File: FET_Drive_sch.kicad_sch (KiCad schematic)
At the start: 14 parts, among them Q15 S8550, Q16 S8050_SMD, Q17 S8050_SMD, Q18 S8050_SMD

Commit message: moree wiring done, shrank board slightly. Unsure whether 4 layer is necessary
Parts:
- added C24, C25: 10u, Capacitor_SMD:C_0603_1608Metric, symbol Device:C_Small
- renumbered D7 to D6, Q18 to Q10, Q15 to Q6, Q16 to Q8, Q17 to Q9, R28 to R19, R54 to R22, R55 to R23, R56 to R24, R57 to R25, R58 to R27, R62 to R59, R63 to R60, R64 to R61
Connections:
- net GND: now also C24.2, C25.2
- new net +12V: C24.1, C25.1
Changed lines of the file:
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@@
   (symbol (lib_id "Device:R_Small_US") (at 168.275 84.455 0) (mirror y)
     (in_bom yes) (on_board yes)
-    (property "Reference" "R56" (id 0) (at 171.45 85.725 0))
+    (property "Reference" "R24" (id 0) (at 171.45 85.725 0))
     (property "Value" "3.3M" (id 1) (at 164.465 84.455 0))
     (property "Footprint" "Resistor_SMD:R_0402_1005Metric" (id 2) (at 168.275 84.455 0)
@@
   (symbol (lib_id "Device:R_Small_US") (at 113.665 86.995 90)
     (in_bom yes) (on_board yes)
-    (property "Reference" "R57" (id 0) (at 113.665 82.1395 90))
+    (property "Reference" "R25" (id 0) (at 113.665 82.1395 90))
     (property "Value" "4k7" (id 1) (at 113.665 84.9146 90))
     (property "Footprint" "Resistor_SMD:R_0402_1005Metric" (id 2) (at 113.665 86.995 0)
@@
     (pin "2")
   )
+  (symbol (lib_id "Device:C_Small") (at 113.03 62.865 0)
+    (in_bom yes) (on_board yes) (fields_autoplaced)
+    (property "Reference" "C25" (id 0) (at 115.3541 61.9628 0)
+      (effects (font (size 1.27 1.27)) (justify left))
+    )
+    (property "Value" "10u" (id 1) (at 115.3541 64.7379 0)
+      (effects (font (size 1.27 1.27)) (justify left))
+    )
+    (property "Footprint" "Capacitor_SMD:C_0603_1608Metric" (id 2) (at 113.03 62.865 0)
+      (effects (font (size 1.27 1.27)) hide)
+    )
+    (property "Datasheet" "~" (id 3) (at 113.03 62.865 0)
+      (effects (font (size 1.27 1.27)) hide)
+    )
+    (property "Populate" "Yes" (id 4) (at 113.03 62.865 0)
+      (effects (font (size 1.27 1.27)) hide)
+    )
+    (property "Extended" "0" (id 5) (at 113.03 62.865 0)
+      (effects (font (size 1.27 1.27)) hide)
+    )
+    (property "LCSC" "C96446" (id 6) (at 113.03 62.865 0)
+      (effects (font (size 1.27 1.27)) hide)
+    )
+    (property "Price" "0.03" (id 7) (at 113.03 62.865 0)
+      (effects (font (size 1.27 1.27)) hide)
+    )
+    (pin "1")
+    (pin "2")
+  )
   (symbol (lib_id "MyDevices:S8050_SMD") (at 137.795 92.075 0)
     (in_bom yes) (on_board yes) (fields_autoplaced)
-    (property "Reference" "Q18" (id 0) (at 141.3764 91.1665 0)
+    (property "Reference" "Q10" (id 0) (at 141.3764 91.1665 0)
       (effects (font (size 1.27 1.27)) (justify left))
     )
@@
   (symbol (lib_id "Device:R_Small_US") (at 155.575 68.58 90)
     (in_bom yes) (on_board yes)
-    (property "Reference" "R62" (id 0) (at 155.575 63.7245 90))
+    (property "Reference" "R59" (id 0) (at 155.575 63.7245 90))
     (property "Value" "100R" (id 1) (at 165.1 66.4996 90))
     (property "Footprint" "Resistor_SMD:R_0402_1005Metric" (id 2) (at 155.575 68.58 0)
@@
     (pin "2")
   )
+  (symbol (lib_id "power:+12V") (at 102.235 60.325 0)
+    (in_bom yes) (on_board yes) (fields_autoplaced)
+    (property "Reference" "#PWR0112" (id 0) (at 102.235 64.135 0)
+      (effects (font (size 1.27 1.27)) hide)
+    )
+    (property "Value" "+12V" (id 1) (at 102.235 56.7205 0))
+    (property "Footprint" "" (id 2) (at 102.235 60.325 0)
+      (effects (font (size 1.27 1.27)) hide)
+    )
+    (property "Datasheet" "" (id 3) (at 102.235 60.325 0)
+      (effects (font (size 1.27 1.27)) hide)
+    )
+    (pin "1")
+  )
   (symbol (lib_id "MyDevices:S8050_SMD") (at 146.685 86.995 0)
     (in_bom yes) (on_board yes) (fields_autoplaced)
-    (property "Reference" "Q17" (id 0) (at 150.2664 86.0865 0)
+    (property "Reference" "Q9" (id 0) (at 150.2664 86.0865 0)
       (effects (font (size 1.27 1.27)) (justify left))
     )
@@
   (symbol (lib_id "Device:R_Small_US") (at 155.575 81.915 90)
     (in_bom yes) (on_board yes)
-    (property "Reference" "R54" (id 0) (at 155.575 77.0595 90))
+    (property "Reference" "R22" (id 0) (at 155.575 77.0595 90))
     (property "Value" "100R" (id 1) (at 165.1 79.8346 90))
     (property "Footprint" "Resistor_SMD:R_0402_1005Metric" (id 2) (at 155.575 81.915 0)
@@
   (symbol (lib_id "MyDevices:S8550") (at 146.685 72.39 0)
     (in_bom yes) (on_board yes) (fields_autoplaced)
-    (property "Reference" "Q15" (id 0) (at 150.2664 71.4815 0)
+    (property "Reference" "Q6" (id 0) (at 150.2664 71.4815 0)
       (effects (font (size 1.27 1.27)) (justify left))
     )
@@
   (symbol (lib_id "Device:R_Small_US") (at 139.065 84.455 180)
     (in_bom yes) (on_board yes)
-    (property "Reference" "R55" (id 0) (at 136.525 85.725 0))
+    (property "Reference" "R23" (id 0) (at 136.525 85.725 0))
     (property "Value" "4k7" (id 1) (at 132.08 83.82 0))
     (property "Footprint" "Resistor_SMD:R_0402_1005Metric" (id 2) (at 139.065 84.455 0)
@@
     (pin "2")
   )
+  (symbol (lib_id "Device:C_Small") (at 102.235 62.865 0)
+    (in_bom yes) (on_board yes) (fields_autoplaced)
+    (property "Reference" "C24" (id 0) (at 104.5591 61.9628 0)
+      (effects (font (size 1.27 1.27)) (justify left))
+    )
+    (property "Value" "10u" (id 1) (at 104.5591 64.7379 0)
+      (effects (font (size 1.27 1.27)) (justify left))
+    )
+    (property "Footprint" "Capacitor_SMD:C_0603_1608Metric" (id 2) (at 102.235 62.865 0)
+      (effects (font (size 1.27 1.27)) hide)
+    )
+    (property "Datasheet" "~" (id 3) (at 102.235 62.865 0)
+      (effects (font (size 1.27 1.27)) hide)
+    )
+    (property "Populate" "Yes" (id 4) (at 102.235 62.865 0)
+      (effects (font (size 1.27 1.27)) hide)
+    )
+    (property "Extended" "0" (id 5) (at 102.235 62.865 0)
+      (effects (font (size 1.27 1.27)) hide)
+    )
+    (property "LCSC" "C96446" (id 6) (at 102.235 62.865 0)
+      (effects (font (size 1.27 1.27)) hide)
+    )
+    (property "Price" "0.03" (id 7) (at 102.235 62.865 0)
+      (effects (font (size 1.27 1.27)) hide)
+    )
+    (pin "1")
+    (pin "2")
+  )
+  (symbol (lib_id "power:+12V") (at 113.03 60.325 0)
+    (in_bom yes) (on_board yes) (fields_autoplaced)
+    (property "Reference" "#PWR0110" (id 0) (at 113.03 64.135 0)
+      (effects (font (size 1.27 1.27)) hide)
+    )
+    (property "Value" "+12V" (id 1) (at 113.03 56.7205 0))
+    (property "Footprint" "" (id 2) (at 113.03 60.325 0)
+      (effects (font (size 1.27 1.27)) hide)
+    )
+    (property "Datasheet" "" (id 3) (at 113.03 60.325 0)
+      (effects (font (size 1.27 1.27)) hide)
+    )
+    (pin "1")
+  )
   (symbol (lib_id "Device:D_Zener_Small") (at 175.26 84.455 270)
     (in_bom yes) (on_board yes)
-    (property "Reference" "D7" (id 0) (at 177.038 83.5465 90)
+    (property "Reference" "D6" (id 0) (at 177.038 83.5465 90)
       (effects (font (size 1.27 1.27)) (justify left))
     )
@@
     (pin "2")
   )
+  (symbol (lib_id "power:GND") (at 102.235 65.405 0)
+    (in_bom yes) (on_board yes) (fields_autoplaced)
+    (property "Reference" "#PWR0113" (id 0) (at 102.235 71.755 0)
+      (effects (font (size 1.27 1.27)) hide)
+    )
+    (property "Value" "GND" (id 1) (at 102.235 69.9675 0))
+    (property "Footprint" "" (id 2) (at 102.235 65.405 0)
+      (effects (font (size 1.27 1.27)) hide)
+    )
+    (property "Datasheet" "" (id 3) (at 102.235 65.405 0)
+      (effects (font (size 1.27 1.27)) hide)
+    )
+    (pin "1")
+  )
   (symbol (lib_id "MyDevices:S8050_SMD") (at 123.825 86.995 0)
     (in_bom yes) (on_board yes) (fields_autoplaced)
-    (property "Reference" "Q16" (id 0) (at 127.4064 86.0865 0)
+    (property "Reference" "Q8" (id 0) (at 127.4064 86.0865 0)
       (effects (font (size 1.27 1.27)) (justify left))
     )
@@
     (pin "3")
   )
+  (symbol (lib_id "power:GND") (at 113.03 65.405 0)
+    (in_bom yes) (on_board yes) (fields_autoplaced)
+    (property "Reference" "#PWR0111" (id 0) (at 113.03 71.755 0)
+      (effects (font (size 1.27 1.27)) hide)
+    )
+    (property "Value" "GND" (id 1) (at 113.03 69.9675 0))
+    (property "Footprint" "" (id 2) (at 113.03 65.405 0)
+      (effects (font (size 1.27 1.27)) hide)
+    )
+    (property "Datasheet" "" (id 3) (at 113.03 65.405 0)
+      (effects (font (size 1.27 1.27)) hide)
+    )
+    (pin "1")
+  )
   (symbol (lib_id "Device:R_Small_US") (at 155.575 77.47 90)
     (in_bom yes) (on_board yes)
-    (property "Reference" "R64" (id 0) (at 155.575 72.6145 90))
+    (property "Reference" "R61" (id 0) (at 155.575 72.6145 90))
     (property "Value" "100R" (id 1) (at 165.1 75.3896 90))
     (property "Footprint" "Resistor_SMD:R_0402_1005Metric" (id 2) (at 155.575 77.47 0)
@@
   (symbol (lib_id "Device:R_Small_US") (at 113.665 95.885 90)
     (in_bom yes) (on_board yes)
-    (property "Reference" "R58" (id 0) (at 113.665 91.0295 90))
+    (property "Reference" "R27" (id 0) (at 113.665 91.0295 90))
     (property "Value" "4k7" (id 1) (at 113.665 93.8046 90))
     (property "Footprint" "Resistor_SMD:R_0402_1005Metric" (id 2) (at 113.665 95.885 0)
@@
   (symbol (lib_id "Device:R_Small_US") (at 135.255 72.39 90)
     (in_bom yes) (on_board yes)
-    (property "Reference" "R28" (id 0) (at 135.255 67.5345 90))
+    (property "Reference" "R19" (id 0) (at 135.255 67.5345 90))
     (property "Value" "4k7" (id 1) (at 135.255 70.3096 90))
     (property "Footprint" "Resistor_SMD:R_0402_1005Metric" (id 2) (at 135.255 72.39 0)
@@
   (symbol (lib_id "Device:R_Small_US") (at 155.575 73.025 90)
     (in_bom yes) (on_board yes)
-    (property "Reference" "R63" (id 0) (at 155.575 68.1695 90))
+    (property "Reference" "R60" (id 0) (at 155.575 68.1695 90))
     (property "Value" "100R" (id 1) (at 165.1 70.9446 90))
     (property "Footprint" "Resistor_SMD:R_0402_1005Metric" (id 2) (at 155.575 73.025 0)

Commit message: got lazy, went 4 layer. Some of layer 3 done. progressing. Mainly committing for board chronological how to sake. Added Caps on the TM1620
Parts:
- renumbered C24 to C26, C25 to C27, D6 to D7, Q6 to Q15, Q8 to Q16, Q9 to Q17, Q10 to Q18, R19 to R28, R22 to R54, R23 to R55, R24 to R56, R25 to R57, R27 to R58, R59 to R62, R60 to R63, R61 to R64
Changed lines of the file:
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@@
   (symbol (lib_id "Device:R_Small_US") (at 168.275 84.455 0) (mirror y)
     (in_bom yes) (on_board yes)
-    (property "Reference" "R24" (id 0) (at 171.45 85.725 0))
+    (property "Reference" "R56" (id 0) (at 171.45 85.725 0))
     (property "Value" "3.3M" (id 1) (at 164.465 84.455 0))
     (property "Footprint" "Resistor_SMD:R_0402_1005Metric" (id 2) (at 168.275 84.455 0)
@@
   (symbol (lib_id "Device:R_Small_US") (at 113.665 86.995 90)
     (in_bom yes) (on_board yes)
-    (property "Reference" "R25" (id 0) (at 113.665 82.1395 90))
+    (property "Reference" "R57" (id 0) (at 113.665 82.1395 90))
     (property "Value" "4k7" (id 1) (at 113.665 84.9146 90))
     (property "Footprint" "Resistor_SMD:R_0402_1005Metric" (id 2) (at 113.665 86.995 0)
@@
   (symbol (lib_id "Device:C_Small") (at 113.03 62.865 0)
     (in_bom yes) (on_board yes) (fields_autoplaced)
-    (property "Reference" "C25" (id 0) (at 115.3541 61.9628 0)
+    (property "Reference" "C27" (id 0) (at 115.3541 61.9628 0)
       (effects (font (size 1.27 1.27)) (justify left))
     )
@@
   (symbol (lib_id "MyDevices:S8050_SMD") (at 137.795 92.075 0)
     (in_bom yes) (on_board yes) (fields_autoplaced)
-    (property "Reference" "Q10" (id 0) (at 141.3764 91.1665 0)
+    (property "Reference" "Q18" (id 0) (at 141.3764 91.1665 0)
       (effects (font (size 1.27 1.27)) (justify left))
     )
@@
   (symbol (lib_id "Device:R_Small_US") (at 155.575 68.58 90)
     (in_bom yes) (on_board yes)
-    (property "Reference" "R59" (id 0) (at 155.575 63.7245 90))
+    (property "Reference" "R62" (id 0) (at 155.575 63.7245 90))
     (property "Value" "100R" (id 1) (at 165.1 66.4996 90))
     (property "Footprint" "Resistor_SMD:R_0402_1005Metric" (id 2) (at 155.575 68.58 0)
@@
   (symbol (lib_id "power:+12V") (at 102.235 60.325 0)
     (in_bom yes) (on_board yes) (fields_autoplaced)
-    (property "Reference" "#PWR0112" (id 0) (at 102.235 64.135 0)
+    (property "Reference" "#PWR0116" (id 0) (at 102.235 64.135 0)
       (effects (font (size 1.27 1.27)) hide)
     )
@@
   (symbol (lib_id "MyDevices:S8050_SMD") (at 146.685 86.995 0)
     (in_bom yes) (on_board yes) (fields_autoplaced)
-    (property "Reference" "Q9" (id 0) (at 150.2664 86.0865 0)
+    (property "Reference" "Q17" (id 0) (at 150.2664 86.0865 0)
       (effects (font (size 1.27 1.27)) (justify left))
     )
@@
   (symbol (lib_id "Device:R_Small_US") (at 155.575 81.915 90)
     (in_bom yes) (on_board yes)
-    (property "Reference" "R22" (id 0) (at 155.575 77.0595 90))
+    (property "Reference" "R54" (id 0) (at 155.575 77.0595 90))
     (property "Value" "100R" (id 1) (at 165.1 79.8346 90))
     (property "Footprint" "Resistor_SMD:R_0402_1005Metric" (id 2) (at 155.575 81.915 0)
@@
   (symbol (lib_id "MyDevices:S8550") (at 146.685 72.39 0)
     (in_bom yes) (on_board yes) (fields_autoplaced)
-    (property "Reference" "Q6" (id 0) (at 150.2664 71.4815 0)
+    (property "Reference" "Q15" (id 0) (at 150.2664 71.4815 0)
       (effects (font (size 1.27 1.27)) (justify left))
     )
@@
   (symbol (lib_id "Device:R_Small_US") (at 139.065 84.455 180)
     (in_bom yes) (on_board yes)
-    (property "Reference" "R23" (id 0) (at 136.525 85.725 0))
+    (property "Reference" "R55" (id 0) (at 136.525 85.725 0))
     (property "Value" "4k7" (id 1) (at 132.08 83.82 0))
     (property "Footprint" "Resistor_SMD:R_0402_1005Metric" (id 2) (at 139.065 84.455 0)
@@
   (symbol (lib_id "Device:C_Small") (at 102.235 62.865 0)
     (in_bom yes) (on_board yes) (fields_autoplaced)
-    (property "Reference" "C24" (id 0) (at 104.5591 61.9628 0)
+    (property "Reference" "C26" (id 0) (at 104.5591 61.9628 0)
       (effects (font (size 1.27 1.27)) (justify left))
     )
@@
   (symbol (lib_id "power:+12V") (at 113.03 60.325 0)
     (in_bom yes) (on_board yes) (fields_autoplaced)
-    (property "Reference" "#PWR0110" (id 0) (at 113.03 64.135 0)
+    (property "Reference" "#PWR0114" (id 0) (at 113.03 64.135 0)
       (effects (font (size 1.27 1.27)) hide)
     )
@@
   (symbol (lib_id "Device:D_Zener_Small") (at 175.26 84.455 270)
     (in_bom yes) (on_board yes)
-    (property "Reference" "D6" (id 0) (at 177.038 83.5465 90)
+    (property "Reference" "D7" (id 0) (at 177.038 83.5465 90)
       (effects (font (size 1.27 1.27)) (justify left))
     )
@@
   (symbol (lib_id "power:GND") (at 102.235 65.405 0)
     (in_bom yes) (on_board yes) (fields_autoplaced)
-    (property "Reference" "#PWR0113" (id 0) (at 102.235 71.755 0)
+    (property "Reference" "#PWR0117" (id 0) (at 102.235 71.755 0)
       (effects (font (size 1.27 1.27)) hide)
     )
@@
   (symbol (lib_id "MyDevices:S8050_SMD") (at 123.825 86.995 0)
     (in_bom yes) (on_board yes) (fields_autoplaced)
-    (property "Reference" "Q8" (id 0) (at 127.4064 86.0865 0)
+    (property "Reference" "Q16" (id 0) (at 127.4064 86.0865 0)
       (effects (font (size 1.27 1.27)) (justify left))
     )
@@
   (symbol (lib_id "power:GND") (at 113.03 65.405 0)
     (in_bom yes) (on_board yes) (fields_autoplaced)
-    (property "Reference" "#PWR0111" (id 0) (at 113.03 71.755 0)
+    (property "Reference" "#PWR0115" (id 0) (at 113.03 71.755 0)
       (effects (font (size 1.27 1.27)) hide)
     )
@@
   (symbol (lib_id "Device:R_Small_US") (at 155.575 77.47 90)
     (in_bom yes) (on_board yes)
-    (property "Reference" "R61" (id 0) (at 155.575 72.6145 90))
+    (property "Reference" "R64" (id 0) (at 155.575 72.6145 90))
     (property "Value" "100R" (id 1) (at 165.1 75.3896 90))
     (property "Footprint" "Resistor_SMD:R_0402_1005Metric" (id 2) (at 155.575 77.47 0)
@@
   (symbol (lib_id "Device:R_Small_US") (at 113.665 95.885 90)
     (in_bom yes) (on_board yes)
-    (property "Reference" "R27" (id 0) (at 113.665 91.0295 90))
+    (property "Reference" "R58" (id 0) (at 113.665 91.0295 90))
     (property "Value" "4k7" (id 1) (at 113.665 93.8046 90))
     (property "Footprint" "Resistor_SMD:R_0402_1005Metric" (id 2) (at 113.665 95.885 0)
@@
   (symbol (lib_id "Device:R_Small_US") (at 135.255 72.39 90)
     (in_bom yes) (on_board yes)
-    (property "Reference" "R19" (id 0) (at 135.255 67.5345 90))
+    (property "Reference" "R28" (id 0) (at 135.255 67.5345 90))
     (property "Value" "4k7" (id 1) (at 135.255 70.3096 90))
     (property "Footprint" "Resistor_SMD:R_0402_1005Metric" (id 2) (at 135.255 72.39 0)
@@
   (symbol (lib_id "Device:R_Small_US") (at 155.575 73.025 90)
     (in_bom yes) (on_board yes)
-    (property "Reference" "R60" (id 0) (at 155.575 68.1695 90))
+    (property "Reference" "R63" (id 0) (at 155.575 68.1695 90))
     (property "Value" "100R" (id 1) (at 165.1 70.9446 90))
     (property "Footprint" "Resistor_SMD:R_0402_1005Metric" (id 2) (at 155.575 73.025 0)

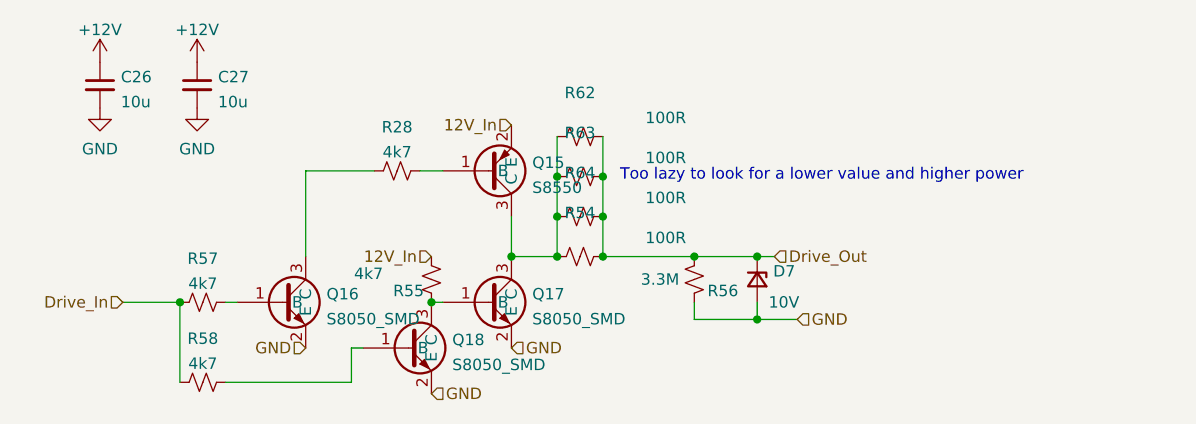
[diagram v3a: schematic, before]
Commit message: major schematic changes, 5V is now the highest voltage, added more FETs for Wire conduction, more for SS, opamp for current hack, removed Regs, XT60 and significantly changed wiring and R values for sections... Still a lot to be done, cant be solved now
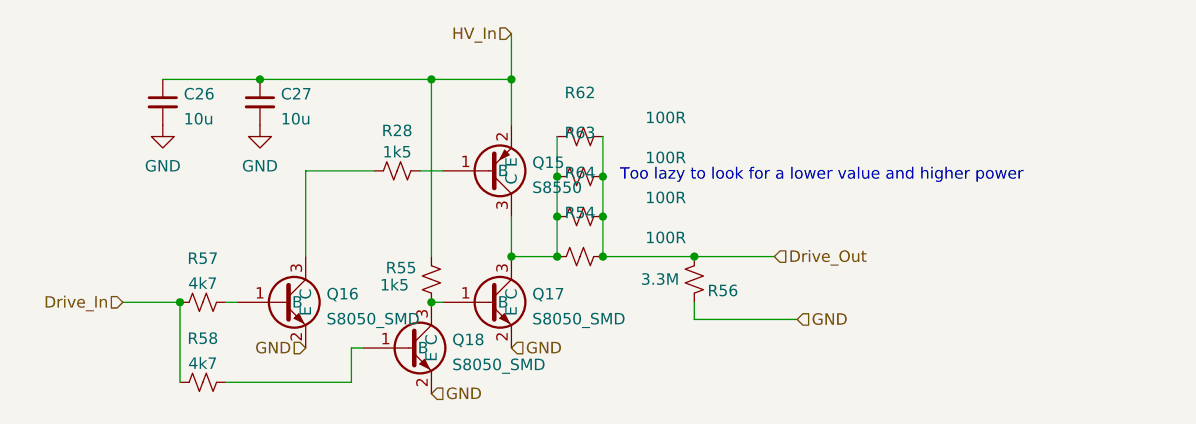
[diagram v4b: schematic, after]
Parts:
- removed D7: 10V, Diode_SMD:D_SOD-123, symbol Device:D_Zener_Small
- R28, R55: value 4k7 -> 1k5; LCSC C25900 -> C25867
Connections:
- net 12V_In is gone; now on net HV_In: Q15.2 (E), R55.2
- net +12V renamed HV_In
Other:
- moved on the sheet: C26, C27
